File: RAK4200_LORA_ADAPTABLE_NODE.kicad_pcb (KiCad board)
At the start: 2 copper layers, 75 x 49 mm, 7 parts, among them U1 RAK4200

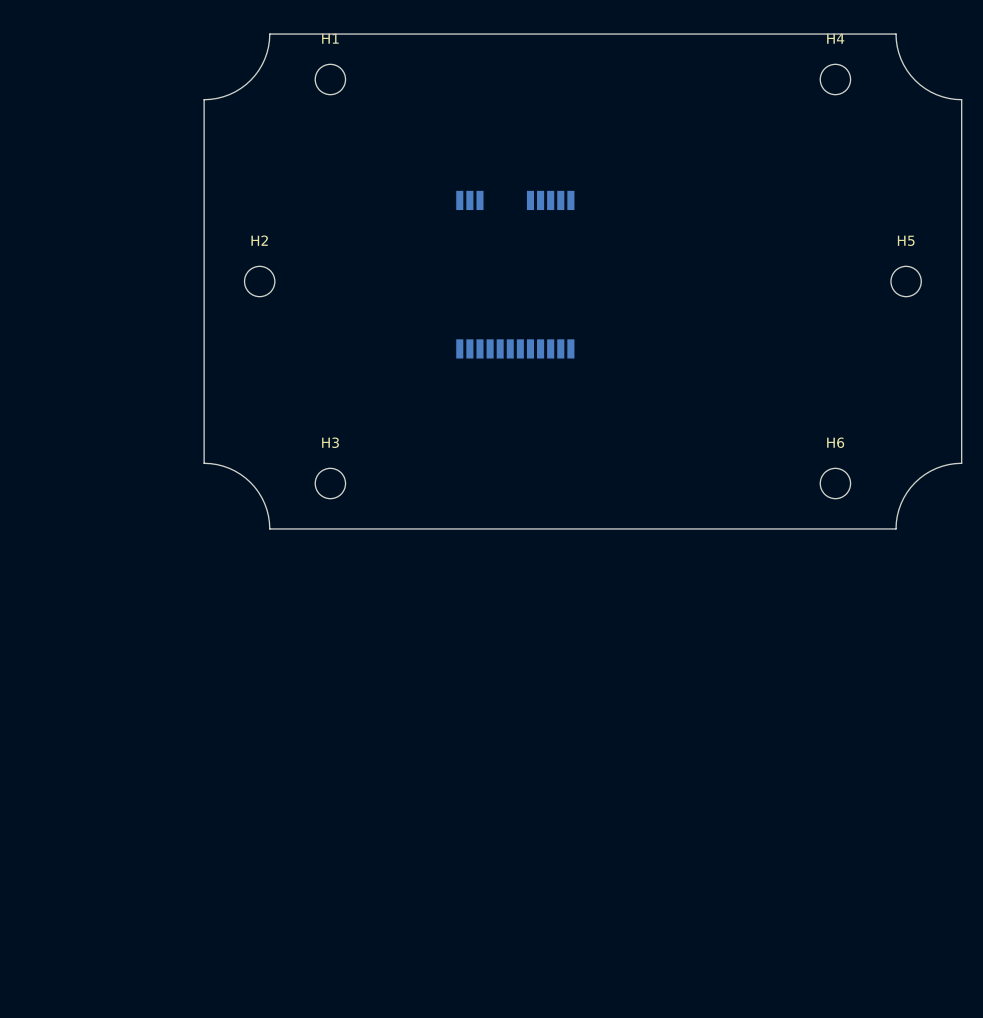
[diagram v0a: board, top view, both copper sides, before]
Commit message: battery holder, solder jumper and screw terminal added
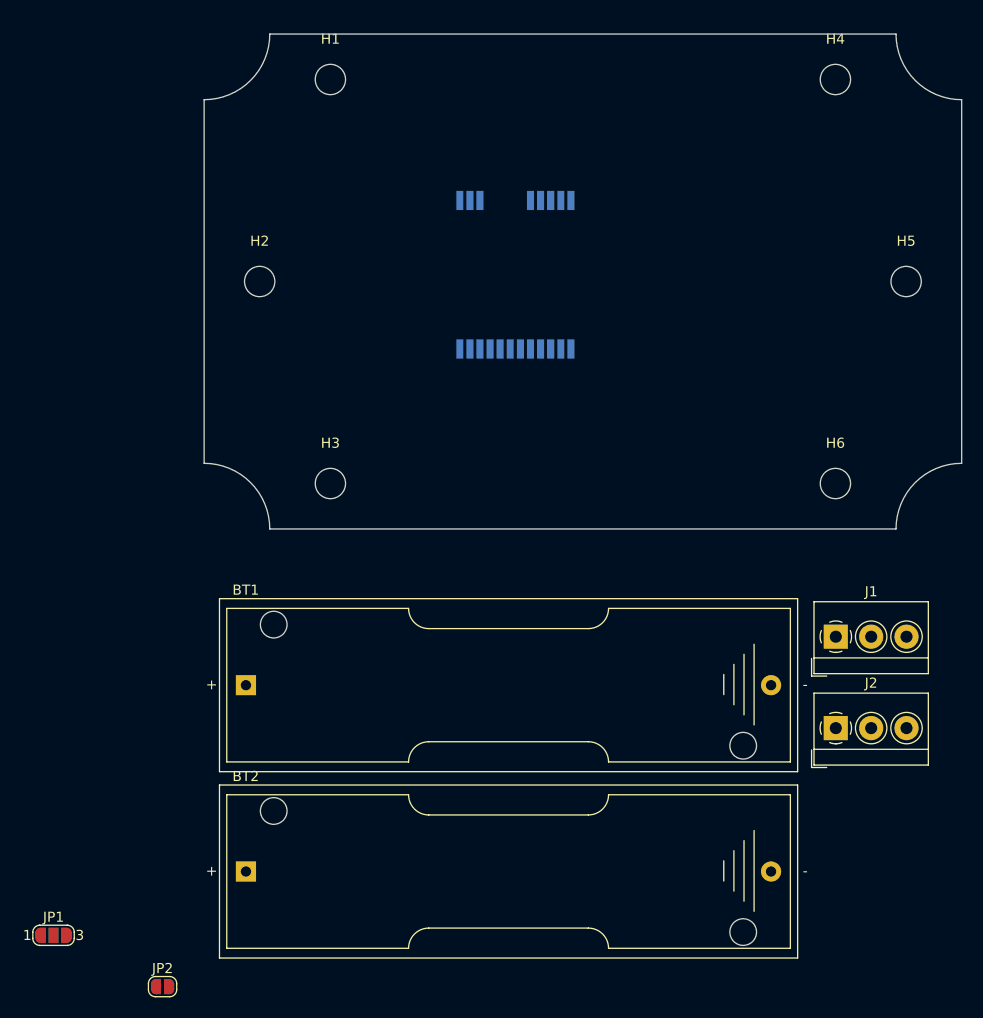
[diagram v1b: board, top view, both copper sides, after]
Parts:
- added BT1: Battery_Cell, Battery:BatteryHolder_Keystone_2460_1xAA, F.Cu at (104.1, 164.5)
- added BT2: Battery_Cell, Battery:BatteryHolder_Keystone_2460_1xAA, F.Cu at (104.1, 182.9)
- added J1: Screw_Terminal_01x03, TerminalBlock_4Ucon:TerminalBlock_4Ucon_1x03_P3.50mm_Horizontal, F.Cu at (162.5, 159.7)
- added J2: Screw_Terminal_01x03, TerminalBlock_4Ucon:TerminalBlock_4Ucon_1x03_P3.50mm_Horizontal, F.Cu at (162.5, 168.7)
- added JP1: SolderJumper_3_Open, Jumper:SolderJumper-3_P1.3mm_Open_RoundedPad1.0x1.5mm_NumberLabels, F.Cu at (85.1, 189.2)
- added JP2: SolderJumper_2_Open, Jumper:SolderJumper-2_P1.3mm_Open_RoundedPad1.0x1.5mm, F.Cu at (95.9, 194.3)

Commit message: expansion connectors added
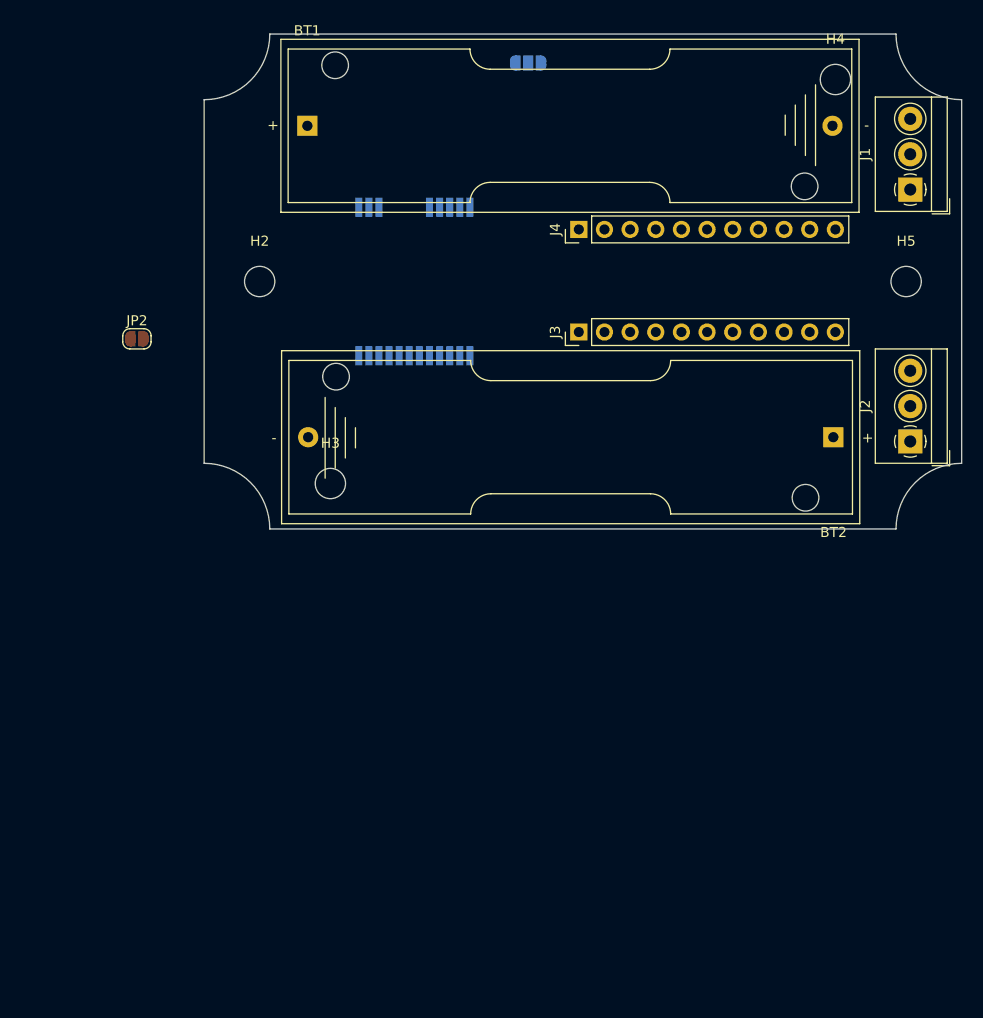
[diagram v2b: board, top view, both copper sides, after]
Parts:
- removed H1, H6: MountingHole, MountingHole:MountingHole_3mm
- added J3: Conn_01x11_Male, Connector_PinHeader_2.54mm:PinHeader_1x11_P2.54mm_Vertical, F.Cu at (137.1, 129.5)
- added J4: Conn_01x11_Male, Connector_PinHeader_2.54mm:PinHeader_1x11_P2.54mm_Vertical, F.Cu at (137.1, 119.3)
- JP1: moved to B.Cu
- moved JP1 98.3 mm to (132.1, 102.9)
- moved BT2 72.3 mm to (162.3, 139.9), turned to 180 degrees
- moved JP2 64.2 mm to (93.3, 130.2)
- moved BT1 55.7 mm to (110.2, 109.1)
- moved J1 44.9 mm to (169.9, 115.4), turned to 90 degrees
- moved J2 29.3 mm to (169.9, 140.3), turned to 90 degrees
- moved U1 10.0 mm to (120.8, 124.5)

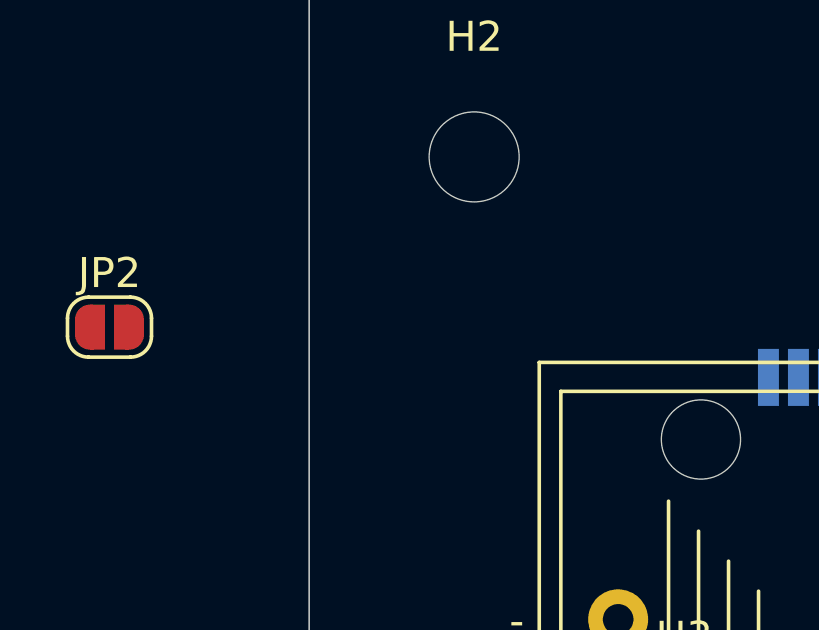
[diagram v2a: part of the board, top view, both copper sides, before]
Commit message: all I/O already connected
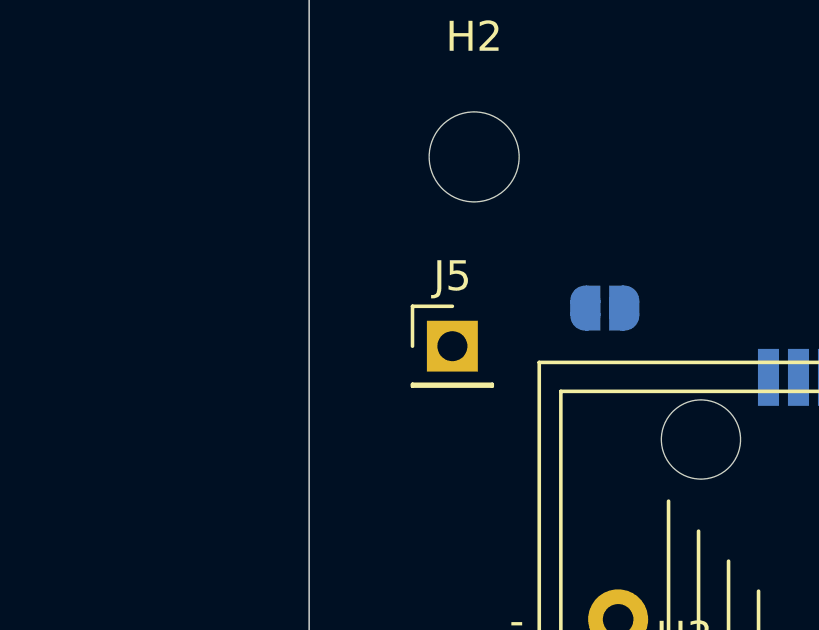
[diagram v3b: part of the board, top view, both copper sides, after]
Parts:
- added J5: Conn_01x01_Male, Connector_PinHeader_2.54mm:PinHeader_1x01_P2.54mm_Vertical, F.Cu at (104.8, 130.8)
- JP2: moved to B.Cu
- moved JP2 16.5 mm to (109.9, 129.5), turned to 180 degrees
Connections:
- J1 pad 2: Net-(J1-Pad2) -> Net-(BT2-Pad2)
- J3 pad 10: Net-(J3-Pad10) -> Net-(J2-Pad2)
- J3 pad 11: Net-(J3-Pad11) -> Net-(J2-Pad3)
- J3 pad 9: Net-(J3-Pad9) -> Net-(J2-Pad1)
- J4 pad 1: Net-(J4-Pad1) -> Net-(J1-Pad3)
- J4 pad 11: Net-(J4-Pad11) -> Net-(J1-Pad1)
- J4 pad 2: Net-(J4-Pad2) -> Net-(BT2-Pad2)
- JP1 pad 2: Net-(JP1-Pad2) -> Net-(J1-Pad3)
- U1 pad 1: Net-(U1-Pad1) -> Net-(J3-Pad1)
- U1 pad 13: Net-(U1-Pad13) -> Net-(BT2-Pad2)
- U1 pad 14: Net-(U1-Pad14) -> Net-(BT2-Pad2)
- U1 pad 15: Net-(U1-Pad15) -> Net-(J4-Pad6)
- U1 pad 16: Net-(U1-Pad16) -> Net-(J4-Pad5)
- U1 pad 17: Net-(U1-Pad17) -> Net-(J4-Pad4)
- U1 pad 18: Net-(U1-Pad18) -> Net-(J4-Pad3)
- U1 pad 19: Net-(U1-Pad19) -> Net-(BT2-Pad2)
- U1 pad 2: Net-(U1-Pad2) -> Net-(J3-Pad2)
- U1 pad 20: Net-(JP1-Pad2) -> Net-(J1-Pad3)
- U1 pad 3: Net-(U1-Pad3) -> Net-(J3-Pad3)
- U1 pad 4: Net-(U1-Pad4) -> Net-(J3-Pad4)
- U1 pad 5: Net-(U1-Pad5) -> Net-(J3-Pad5)
- U1 pad 6: Net-(U1-Pad6) -> Net-(J3-Pad6)
- U1 pad 7: Net-(U1-Pad7) -> Net-(J3-Pad7)
- U1 pad 8: Net-(U1-Pad8) -> Net-(J3-Pad8)

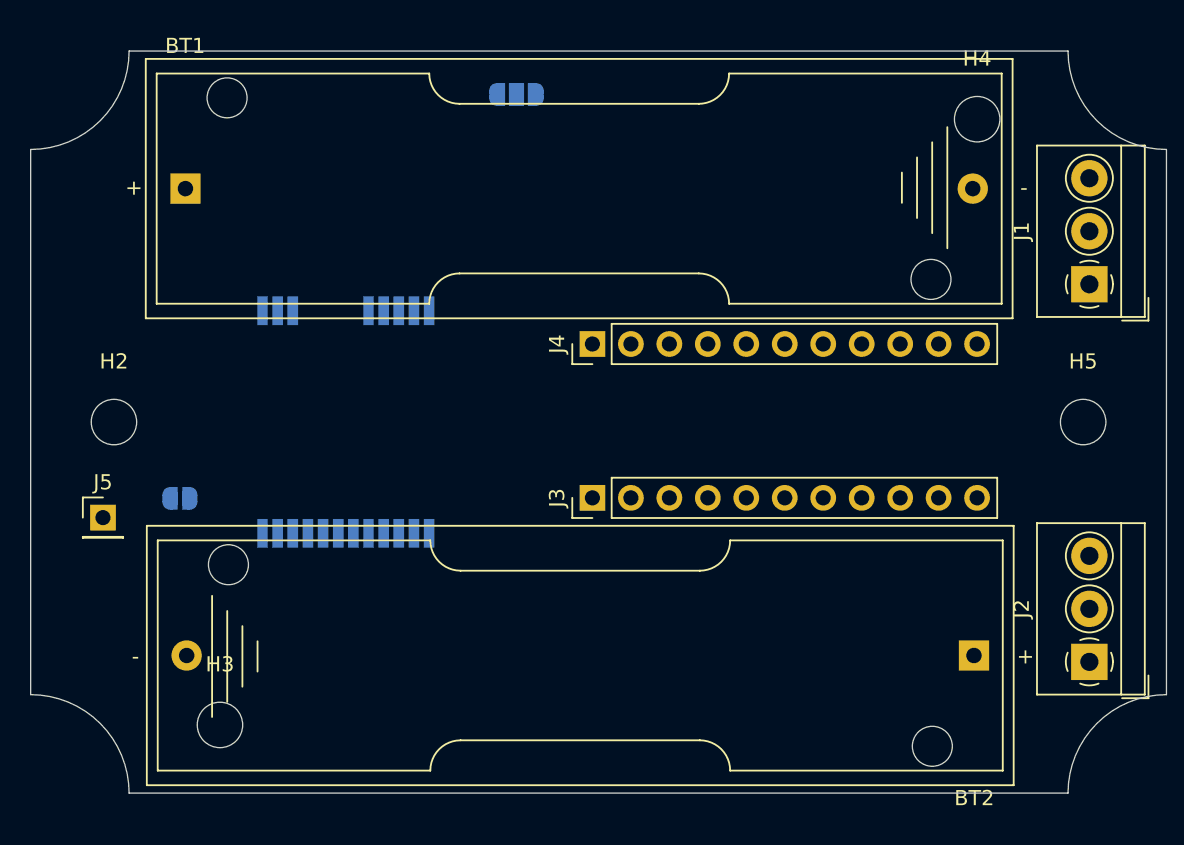
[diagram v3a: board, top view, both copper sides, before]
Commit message: all traces routed
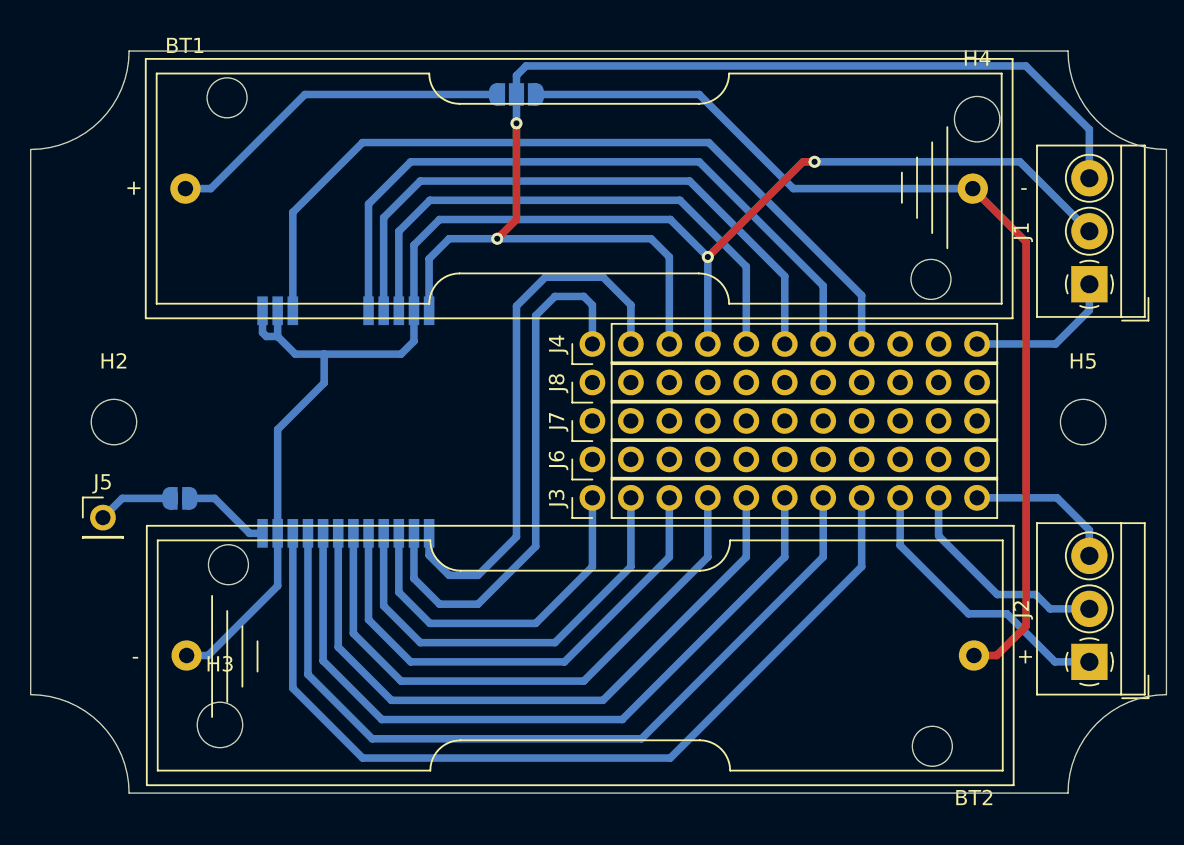
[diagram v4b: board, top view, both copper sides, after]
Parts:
- added J6: Conn_01x11_Male, Connector_PinHeader_2.54mm:PinHeader_1x11_P2.54mm_Vertical, F.Cu at (137.1, 127.0)
- added J7: Conn_01x11_Male, Connector_PinHeader_2.54mm:PinHeader_1x11_P2.54mm_Vertical, F.Cu at (137.1, 124.4)
- added J8: Conn_01x11_Male, Connector_PinHeader_2.54mm:PinHeader_1x11_P2.54mm_Vertical, F.Cu at (137.1, 121.9)
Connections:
- J4 pad 1: Net-(J1-Pad3) -> Net-(J4-Pad1)
- J4 pad 2: Net-(BT2-Pad2) -> Net-(J4-Pad2)
- J4 pad 3: Net-(J4-Pad3) -> Net-(J1-Pad3)
- J4 pad 4: Net-(J4-Pad4) -> Net-(BT2-Pad2)
- U1 pad 1: Net-(J3-Pad1) -> Net-(J4-Pad2)
- U1 pad 10: Net-(U1-Pad10) -> Net-(J3-Pad8)
- U1 pad 15: Net-(J4-Pad6) -> Net-(J4-Pad8)
- U1 pad 16: Net-(J4-Pad5) -> Net-(J4-Pad7)
- U1 pad 17: Net-(J4-Pad4) -> Net-(J4-Pad6)
- U1 pad 18: Net-(J4-Pad3) -> Net-(J4-Pad5)
- U1 pad 2: Net-(J3-Pad2) -> Net-(J4-Pad1)
- U1 pad 3: Net-(J3-Pad3) -> Net-(J3-Pad1)
- U1 pad 4: Net-(J3-Pad4) -> Net-(J3-Pad2)
- U1 pad 5: Net-(J3-Pad5) -> Net-(J3-Pad3)
- U1 pad 6: Net-(J3-Pad6) -> Net-(J3-Pad4)
- U1 pad 7: Net-(J3-Pad7) -> Net-(J3-Pad5)
- U1 pad 8: Net-(J3-Pad8) -> Net-(J3-Pad6)
- U1 pad 9: Net-(U1-Pad9) -> Net-(J3-Pad7)
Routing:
- net Net-(BT2-Pad2): track 0.00 -> 101.5 mm, vias 0 -> 2
- net Net-(J1-Pad3): track 0.00 -> 80.4 mm, vias 0 -> 2
- net Net-(BT1-Pad2): track 0.00 -> 66.0 mm
- net Net-(J3-Pad8): track 0.00 -> 59.5 mm
- net Net-(J3-Pad7): track 0.00 -> 54.0 mm
- net Net-(J4-Pad8): track 0.00 -> 53.4 mm
- net Net-(J3-Pad6): track 0.00 -> 48.9 mm
- net Net-(J4-Pad7): track 0.00 -> 45.5 mm
- net Net-(J3-Pad5): track 0.00 -> 43.7 mm
- net Net-(J4-Pad6): track 0.00 -> 40.7 mm
- net Net-(J3-Pad4): track 0.00 -> 38.6 mm
- net Net-(J4-Pad5): track 0.00 -> 36.0 mm
- net Net-(J4-Pad2): track 0.00 -> 35.7 mm
- net Net-(J4-Pad1): track 0.00 -> 35.6 mm
- net Net-(J3-Pad3): track 0.00 -> 33.5 mm
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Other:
- net class Default: trace_width 0.25 -> 0.5

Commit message: all silks msg done
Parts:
- added REF**: OSHW-Symbol_6.7x6mm_SilkScreen, Symbol:OSHW-Symbol_6.7x6mm_SilkScreen, B.Cu at (137.8, 140.3)
- added REF**: OSHW-Symbol_6.7x6mm_Copper, Symbol:OSHW-Symbol_6.7x6mm_Copper, F.Cu at (128.9, 123.8)
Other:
- board text added: "JP1 BATT 1-2 BT1+BT2 2-3 BT2"
- board text added: "JP2 ANT 1-2 J6"
- board text added: "RAK4200 LORA ADAPTABLE NODE V 0"
- board text added: "W X Y"
- board text added: "Z GND VCC"
